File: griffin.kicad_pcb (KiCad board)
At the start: 2 copper layers, 150 x 100 mm, 43 parts, among them IC1 ME6211C33M5G-N, J1 USB_B_Micro, J2 Conn_02x03_Odd_Even, J3 Conn_01x04, J4 Conn_01x11, J5 Conn_01x04, J6 Conn_01x20, J7 Conn_01x20, J8 Conn_01x14, J9 Conn_01x08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

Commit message: remove _autosave-griffin.sch from .gitignore
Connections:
- C11 pad 2: Net-(C11-Pad2) -> /+3.3V
- C12 pad 2: Net-(C11-Pad2) -> /+3.3V
- IC1 pad 5: Net-(C11-Pad2) -> /+3.3V
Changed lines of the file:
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@@
     (zones 0)
     (modules 43)
-    (nets 54)
+    (nets 53)
   )
   (page A4)
@@
   (net 50 "Net-(J1-Pad1)")
   (net 51 /+3.3V)
-  (net 52 "Net-(C11-Pad2)")
-  (net 53 /BOOT0)
+  (net 52 /BOOT0)
   (net_class Default "This is the default net class."
     (clearance 0.2)
@@
     (add_net GND)
     (add_net "Net-(C10-Pad1)")
-    (add_net "Net-(C11-Pad2)")
     (add_net "Net-(C3-Pad2)")
     (add_net "Net-(C4-Pad2)")
@@
     (pad 4 smd rect (at 1.25 0.95 90) (size 0.6 1.4) (layers F.Cu F.Paste F.Mask))
     (pad 5 smd rect (at 1.25 -0.95 90) (size 0.6 1.4) (layers F.Cu F.Paste F.Mask)
-      (net 52 "Net-(C11-Pad2)"))
+      (net 51 /+3.3V))
     (model ME6211C33M5G-N.stp
       (at (xyz 0 0 0))
@@
       (net 22 /PB7))
     (pad 44 smd roundrect (at -0.75 -4.1625 135) (size 0.3 1.475) (layers F.Cu F.Paste F.Mask) (roundrect_rratio 0.25)
-      (net 53 /BOOT0))
+      (net 52 /BOOT0))
     (pad 45 smd roundrect (at -1.25 -4.1625 135) (size 0.3 1.475) (layers F.Cu F.Paste F.Mask) (roundrect_rratio 0.25)
       (net 21 /PB8))
@@
       (net 15 "Net-(J2-Pad3)"))
     (pad 1 smd roundrect (at -0.825 0) (size 0.8 0.95) (layers F.Cu F.Paste F.Mask) (roundrect_rratio 0.25)
-      (net 53 /BOOT0))
+      (net 52 /BOOT0))
     (model ${KISYS3DMOD}/Resistor_SMD.3dshapes/R_0603_1608Metric.wrl
       (at (xyz 0 0 0))
@@
       (net 1 GND))
     (pad 2 smd roundrect (at 0.775 0) (size 0.9 0.95) (layers F.Cu F.Paste F.Mask) (roundrect_rratio 0.25)
-      (net 52 "Net-(C11-Pad2)"))
+      (net 51 /+3.3V))
     (model ${KISYS3DMOD}/Capacitor_SMD.3dshapes/C_0603_1608Metric.wrl
       (at (xyz 0 0 0))
@@
     )
     (pad 2 smd roundrect (at 0.775 0) (size 0.9 0.95) (layers F.Cu F.Paste F.Mask) (roundrect_rratio 0.25)
-      (net 52 "Net-(C11-Pad2)"))
+      (net 51 /+3.3V))
     (pad 1 smd roundrect (at -0.775 0) (size 0.9 0.95) (layers F.Cu F.Paste F.Mask) (roundrect_rratio 0.25)
       (net 1 GND))

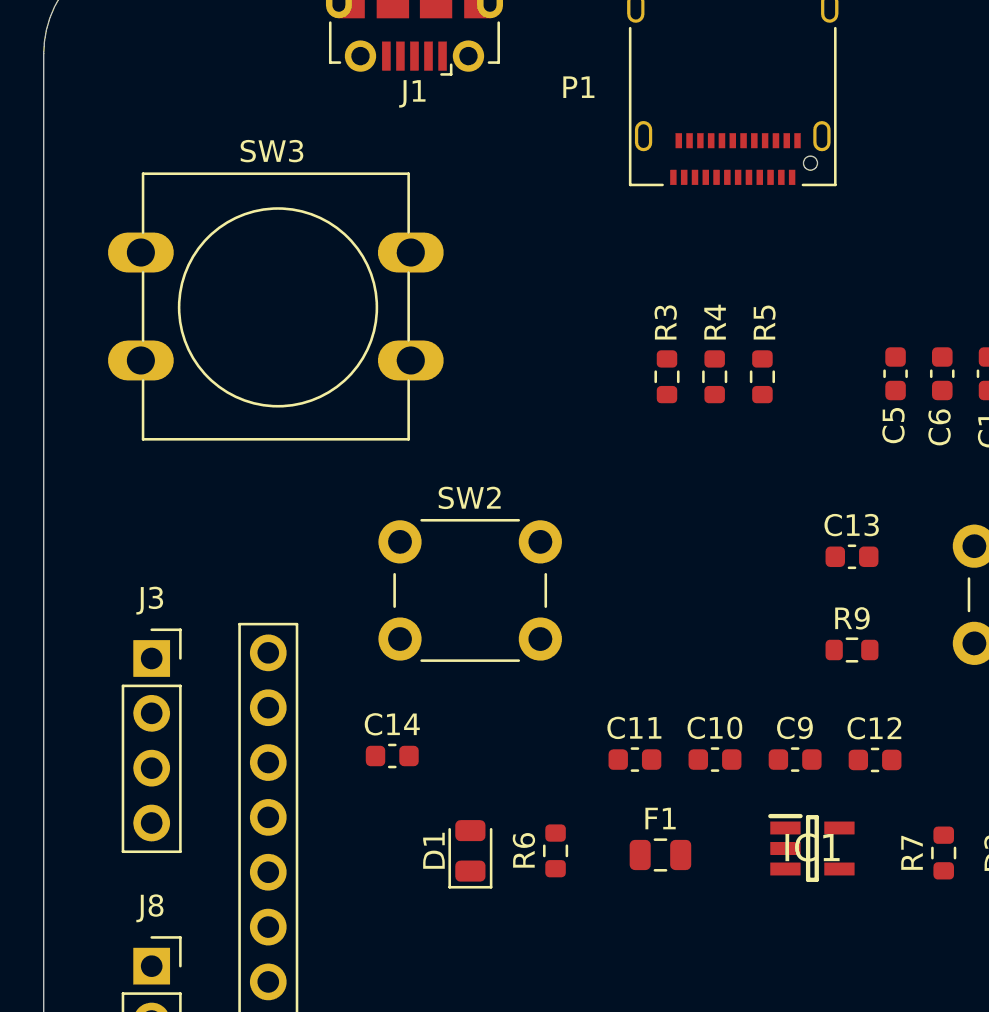
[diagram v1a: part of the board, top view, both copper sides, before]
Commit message: Add cabling rules
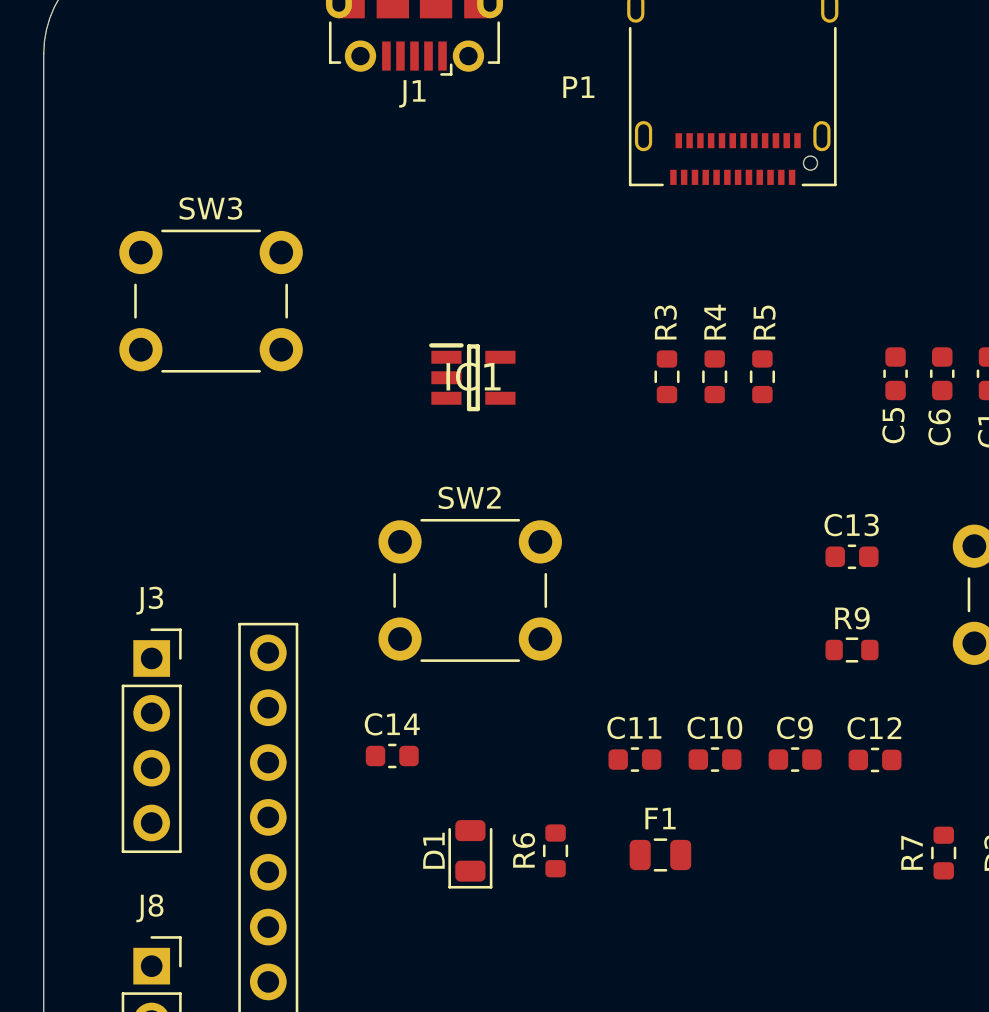
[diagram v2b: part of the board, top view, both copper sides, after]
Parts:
- SW3: footprint Button_Switch_THT:SW_PUSH-12mm -> Button_Switch_THT:SW_PUSH_6mm
- moved IC1 26.9 mm to (61.9, 61.0)

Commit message: finish PCB layout
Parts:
- removed P1: USB_C_Plug, Connector_USB:USB_C_Receptacle_Amphenol_12401610E4-2A
- removed SW3: SW_Push, Button_Switch_THT:SW_PUSH_6mm
- moved C3 44.0 mm to (100.3, 132.8), turned to 90 degrees
- moved C4 42.1 mm to (103.4, 132.8), turned to 90 degrees
- moved Y1 40.2 mm to (107.4, 132.6), turned to 90 degrees
- moved F1 30.3 mm to (69.2, 52.8), turned to 90 degrees
- moved C12 30.2 mm to (58.0, 58.6), turned to 270 degrees
- moved C2 28.8 mm to (60.1, 68.1), turned to 90 degrees
- moved C1 24.7 mm to (62.2, 68.1), turned to 90 degrees
- moved C11 21.6 mm to (61.3, 58.6), turned to 270 degrees
- moved R8 21.4 mm to (47.5, 136.9)
- moved J2 21.4 mm to (60.6, 136.7)
- moved R2 21.4 mm to (47.4, 140.0)
- moved C6 20.6 mm to (64.4, 68.1), turned to 90 degrees
- moved C9 20.1 mm to (75.5, 58.6), turned to 270 degrees
- moved C10 20.1 mm to (71.5, 58.6), turned to 270 degrees
- moved D2 20.0 mm to (90.5, 63.2)
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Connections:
- J1 pad 1: Net-(J1-Pad1) -> +5V
- J1 pad 2: Net-(J1-Pad2) -> /D-
- J1 pad 3: Net-(J1-Pad3) -> /D+
- R3 pad 2: Net-(J1-Pad3) -> /D-
- R4 pad 2: Net-(J1-Pad3) -> /D+
- R5 pad 2: Net-(J1-Pad2) -> /D-
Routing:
- net GND: track 0.00 -> 273.6 mm, vias 0 -> 6
- net /+3.3V: track 0.00 -> 93.2 mm
- net /KEY0: track 0.00 -> 78.3 mm, vias 0 -> 2
- net /PB12: track 0.00 -> 31.1 mm
- net /PB13: track 0.00 -> 28.3 mm
- net /PB14: track 0.00 -> 27.0 mm
- net /PB11: track 0.00 -> 26.8 mm
- net /PB15: track 0.00 -> 25.8 mm
- net /VBAT: track 0.00 -> 25.7 mm
- net /PB10: track 0.00 -> 25.6 mm
- net /PB9: track 0.00 -> 25.4 mm
- net Net-(C8-Pad2): track 0.00 -> 25.0 mm, vias 0 -> 2
- net Net-(C7-Pad2): track 0.00 -> 24.5 mm, vias 0 -> 2
- net /LED2: track 0.00 -> 24.4 mm
- net /BOOT1: track 0.00 -> 24.3 mm
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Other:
- net class Default: clearance 0.2 -> 0.15
- rule pad_to_mask_clearance: 0 -> 0.05
- rule trace_clearance: 0.2 -> 0.15

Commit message: finish PCB layout
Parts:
- moved C14 47.6 mm to (64.2, 117.3), turned to 180 degrees
- moved R8 38.7 mm to (85.0, 127.5)
- moved C4 25.0 mm to (83.4, 117.8)
- moved C3 25.0 mm to (80.3, 117.8)
- moved Y1 25.0 mm to (87.4, 117.6), turned to 180 degrees
- moved R2 21.2 mm to (64.8, 127.7)
- moved J2 17.2 mm to (73.4, 125.1), turned to 0 degrees
- moved R9 12.5 mm to (90.3, 64.3)
- moved C13 10.3 mm to (90.2, 68.1), turned to 180 degrees
- moved D2 5.98 mm to (84.9, 65.3)
- moved R7 5.98 mm to (80.8, 65.3)
- moved D1 3.98 mm to (72.2, 65.3)
- moved R6 3.98 mm to (76.1, 65.3)
- moved J9 3.20 mm to (66.4, 136.2)
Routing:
- net GND: track 273.6 -> 421.8 mm, vias 6 -> 11
- net /+3.3V: track 93.2 -> 219.3 mm, vias 0 -> 8
- net /RESET: track 0.00 -> 118.8 mm
- net /PA14: track 0.00 -> 110.0 mm, vias 0 -> 1
- net /LED2: track 24.4 -> 85.5 mm, vias 0 -> 2
- net /BOOT1: track 24.3 -> 73.7 mm, vias 0 -> 2
- net /PA7: track 0.00 -> 44.9 mm, vias 0 -> 1
- net Net-(C4-Pad2): track 0.00 -> 41.3 mm, vias 0 -> 2
- net /PA13: track 0.00 -> 38.1 mm
- net /BOOT0: track 0.00 -> 35.1 mm, vias 0 -> 2
- net Net-(C3-Pad2): track 0.00 -> 27.8 mm, vias 0 -> 2
- net /PA5: track 19.2 -> 40.4 mm, vias 0 -> 3
- net /VBAT: track 25.7 -> 44.7 mm
- net Net-(J1-Pad6): track 0.00 -> 18.2 mm
- net Net-(C8-Pad2): track 25.0 -> 39.8 mm, vias 2 -> 4
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- added copper zone on F.Cu, net (none)

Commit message: generate gerber files
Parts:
- added G***: LOGO, griffin:hank-solder, B.Cu at (112.0, 117.5)
- added G***: LOGO, griffin:hank-solder, F.Cu at (159.6, 107.6)
- added G***: LOGO, griffin:hank-silk, F.Cu at (177.5, 107.5)
- added REF**: BatteryHolder_Keystone_105_1x2430, Battery:BatteryHolder_Keystone_105_1x2430, B.Cu at (127.5, 112.2)
- added REF**: USB_C_Receptacle_GCT_USB4085, Connector_USB:USB_C_Receptacle_GCT_USB4085, F.Cu at (182.9, 114.3)
- added REF**: USB_C_Receptacle_Amphenol_12401610E4-2A_CircularHoles, Connector_USB:USB_C_Receptacle_Amphenol_12401610E4-2A_CircularHoles, B.Cu at (186.3, 99.9)
- added REF**: USB_C_Receptacle_Amphenol_12401610E4-2A, Connector_USB:USB_C_Receptacle_Amphenol_12401610E4-2A, B.Cu at (186.3, 88.5)
- added REF**: Wifi_Module_ESP8266_WRL-13678, digikey-footprints:Wifi_Module_ESP8266_WRL-13678, F.Cu at (160.2, 69.7)
- added REF**: WIFI_Module_ESP8266_2491, digikey-footprints:WIFI_Module_ESP8266_2491, F.Cu at (181.0, 71.4)
- added REF**: ESP32-WROOM-32D, digikey-footprints:ESP32-WROOM-32D, F.Cu at (156.1, 50.7)
- added REF**: Adafruit_SSD1306, Display:Adafruit_SSD1306, F.Cu at (117.2, 47.0)
- added hank: LOGO, griffin:hank-silk, B.Cu at (142.8, 122.0)
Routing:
- net (no net): vias 0 -> 2
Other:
- board text added: "https://uinika.gitee.io/"
- board text added: "https://www.zhihu.com/people/uinika"
